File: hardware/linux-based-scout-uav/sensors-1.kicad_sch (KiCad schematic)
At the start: 1 part, among them U5 MPU-6050

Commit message: Schematic update
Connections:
- net I2C1_SCL: now reaches U5.23 (SCL)
- net I2C1_SDA: now reaches U5.24 (SDA)
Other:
- note added: "Sensors"
- moved on the sheet: U5
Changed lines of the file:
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@@
 	(wire
 		(pts
-			(xy 228.6 157.48) (xy 228.6 170.18)
+			(xy 92.71 148.59) (xy 92.71 161.29)
 		)
 		(stroke
@@
 		)
 	)
+	(wire
+		(pts
+			(xy 57.15 123.19) (xy 74.93 123.19)
+		)
+		(stroke
+			(width 0)
+			(type default)
+		)
+	)
+	(wire
+		(pts
+			(xy 57.15 125.73) (xy 74.93 125.73)
+		)
+		(stroke
+			(width 0)
+			(type default)
+		)
+	)
+	(text "Sensors"
+		(exclude_from_sim no)
+		(at 213.36 32.766 0)
+		(effects
+			(font
+				(face "KiCad Font")
+				(size 10.16 10.16)
+			)
+		)
+	)
+	(global_label "I2C1_SDA"
+		(shape bidirectional)
+		(at 57.15 123.19 180)
+		(fields_autoplaced yes)
+		(effects
+			(font
+				(size 1.27 1.27)
+			)
+			(justify right)
+		)
+		(property "Intersheetrefs" "${INTERSHEET_REFS}"
+			(at 44.224 123.19 0)
+			(effects
+				(font
+					(size 1.27 1.27)
+				)
+				(justify right)
+				(hide yes)
+			)
+		)
+	)
+	(global_label "I2C1_SCL"
+		(shape input)
+		(at 57.15 125.73 180)
+		(fields_autoplaced yes)
+		(effects
+			(font
+				(size 1.27 1.27)
+			)
+			(justify right)
+		)
+		(property "Intersheetrefs" "${INTERSHEET_REFS}"
+			(at 45.3958 125.73 0)
+			(effects
+				(font
+					(size 1.27 1.27)
+				)
+				(justify right)
+				(hide yes)
+			)
+		)
+	)
 	(symbol
 		(lib_id "Sensor_Motion:MPU-6050")
-		(at 228.6 139.7 0)
+		(at 92.71 130.81 0)
 		(unit 1)
 		(exclude_from_sim no)
@@
 		(fields_autoplaced yes)
 		(property "Reference" "U5"
-			(at 230.7941 156.21 0)
+			(at 94.9041 147.32 0)
 			(effects
 				(font
@@
 		)
 		(property "Value" "MPU-6050"
-			(at 230.7941 158.75 0)
+			(at 94.9041 149.86 0)
 			(effects
 				(font
@@
 		)
 		(property "Footprint" "Sensor_Motion:InvenSense_QFN-24_4x4mm_P0.5mm"
-			(at 228.6 160.02 0)
+			(at 92.71 151.13 0)
 			(effects
 				(font
@@
 		)
 		(property "Datasheet" "https://invensense.tdk.com/wp-content/uploads/2015/02/MPU-6000-Datasheet1.pdf"
-			(at 228.6 143.51 0)
+			(at 92.71 134.62 0)
 			(effects
 				(font
@@
 		)
 		(property "Description" "InvenSense 6-Axis Motion Sensor, Gyroscope, Accelerometer, I2C"
-			(at 228.6 139.7 0)
+			(at 92.71 130.81 0)
 			(effects
 				(font
@@
 	(symbol
 		(lib_id "power:GND")
-		(at 228.6 170.18 0)
+		(at 92.71 161.29 0)
 		(unit 1)
 		(exclude_from_sim no)
@@
 		(fields_autoplaced yes)
 		(property "Reference" "#PWR017"
-			(at 228.6 176.53 0)
+			(at 92.71 167.64 0)
 			(effects
 				(font
@@
 		)
 		(property "Value" "GND"
-			(at 228.6 175.26 0)
+			(at 92.71 166.37 0)
 			(effects
 				(font
@@
 		)
 		(property "Footprint" ""
-			(at 228.6 170.18 0)
+			(at 92.71 161.29 0)
 			(effects
 				(font
@@
 		)
 		(property "Datasheet" ""
-			(at 228.6 170.18 0)
+			(at 92.71 161.29 0)
 			(effects
 				(font
@@
 		)
 		(property "Description" "Power symbol creates a global label with name \"GND\" , ground"
-			(at 228.6 170.18 0)
-			(effects
-				(font
+			(at 92.71 161.29 0)
+			(effects
+				(font

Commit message: Schematic update
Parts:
- added R10: 10K, Resistor_SMD:R_0402_1005Metric, symbol Device:R
- added R11, R12: 10K DNP, Resistor_SMD:R_0402_1005Metric, symbol Device:R
- added U6: AMG8833, AMG8833:XDCR_AMG8833, symbol AMG8833:AMG8833
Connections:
- net GND: now also R11.2, U6.6 (GND)
- new net: R12.2, U6.4 (INT)
- new net: R10.2, R11.1, U6.5 (AD_SELECT)
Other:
- note added: "MPU-6050"
- moved on the sheet: U5

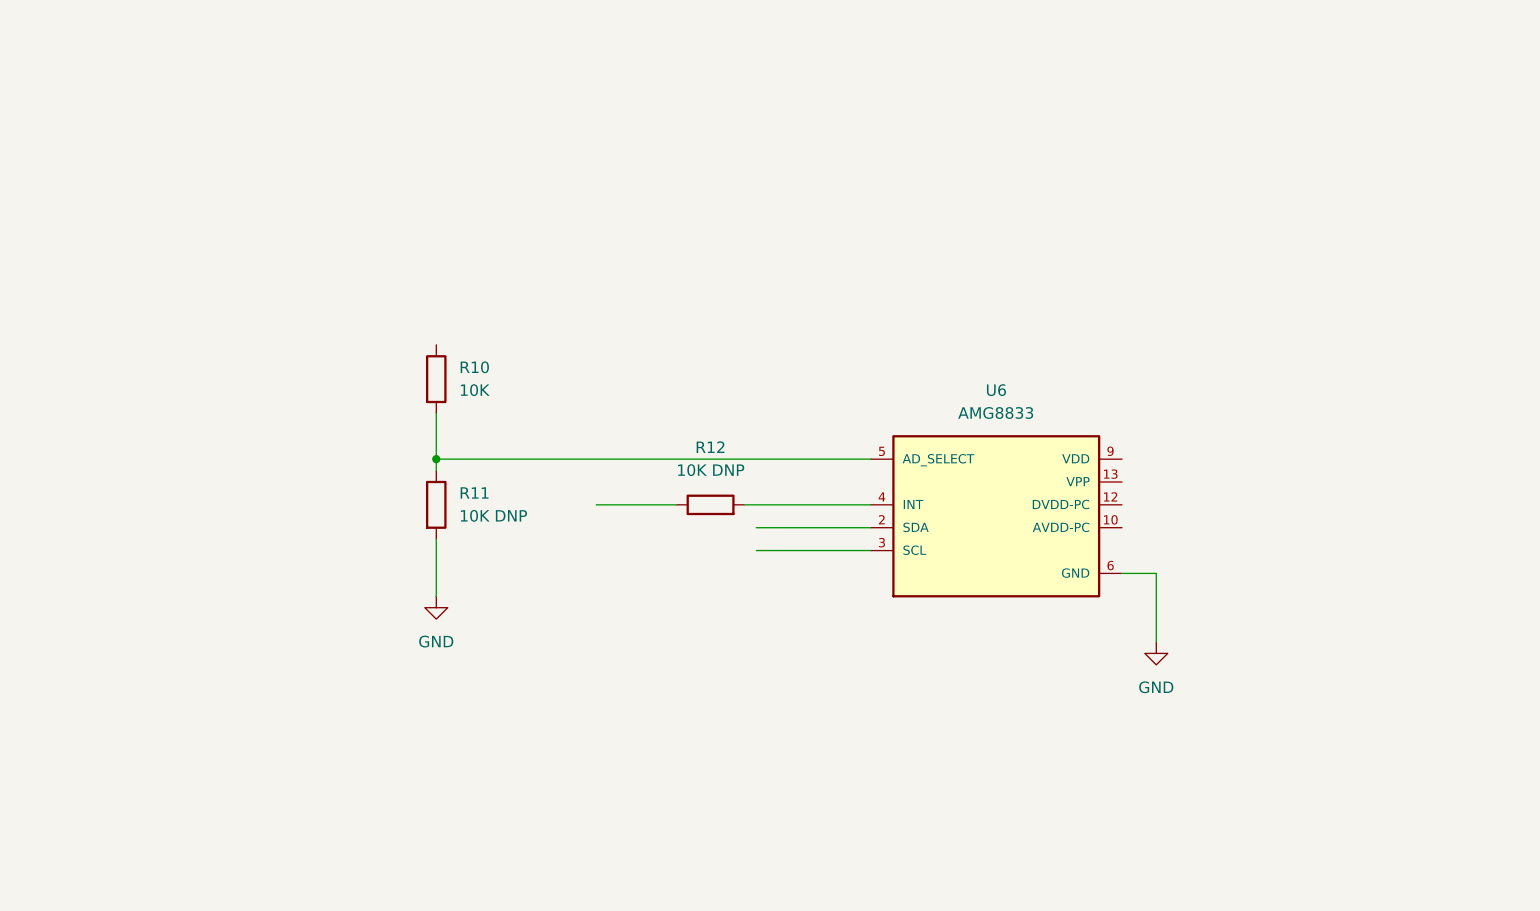
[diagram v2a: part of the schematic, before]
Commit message: Shcematic, board update.
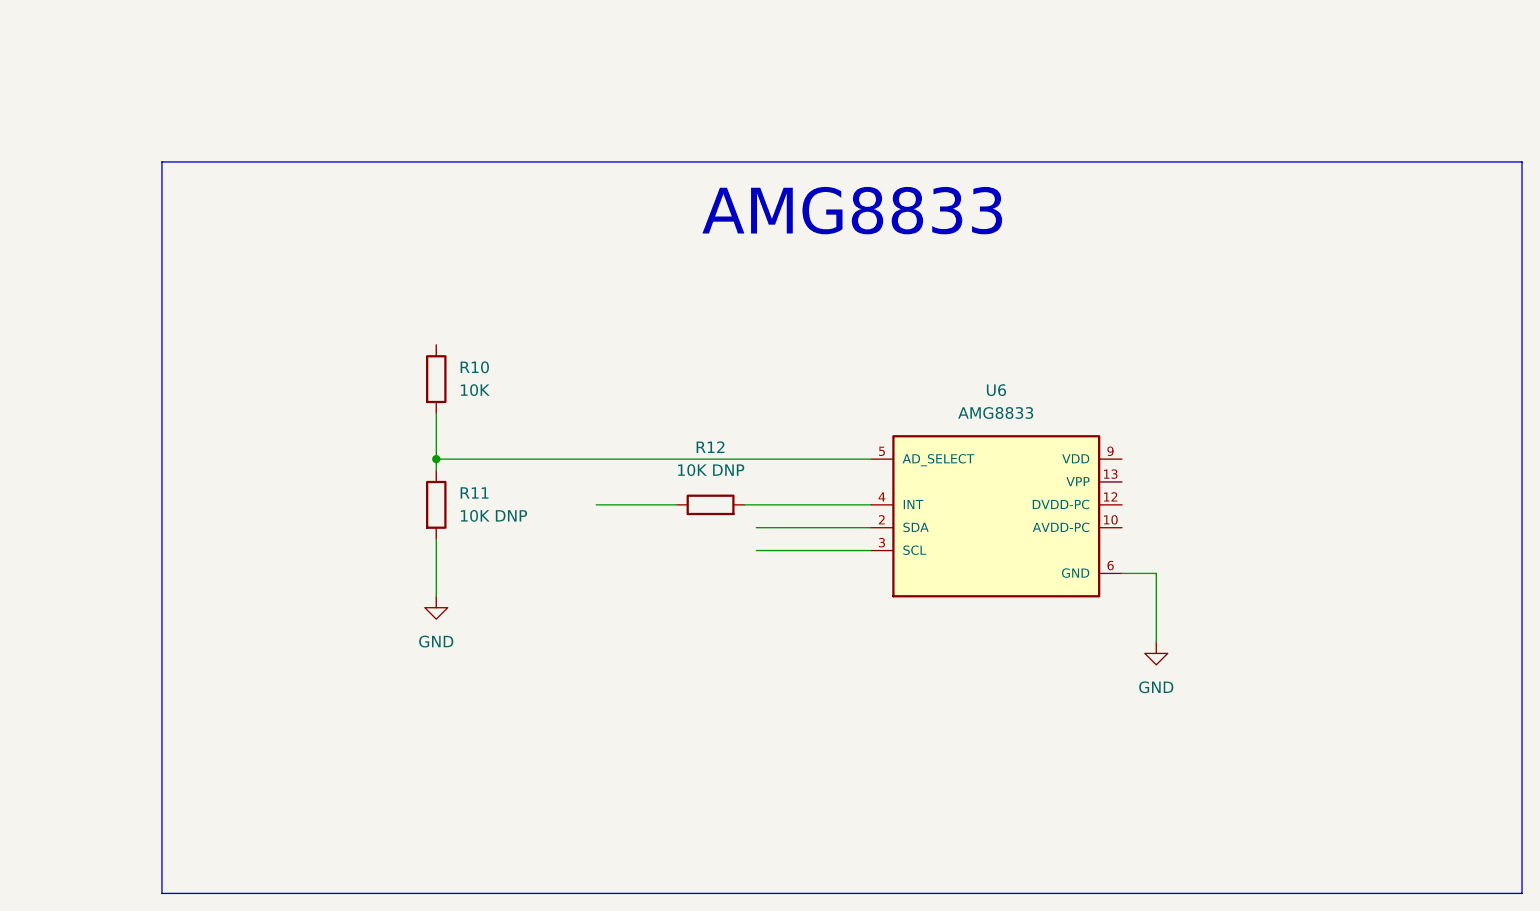
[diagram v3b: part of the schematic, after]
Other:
- note added: "AMG8833"
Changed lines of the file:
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@@
+		)
+	)
+	(rectangle
+		(start 195.58 92.71)
+		(end 346.71 173.99)
+		(stroke
+			(width 0)
+			(type default)
+		)
+		(fill
+			(type none)
+		)
+	)
+	(text "AMG8833"
+		(exclude_from_sim no)
+		(at 272.542 98.552 0)
+		(effects
+			(font
+				(size 5.08 5.08)
+			)
 		)
 	)

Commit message: Schematic update
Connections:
- net I2C1_SCL: now also U6.3 (SCL)
- net I2C1_SDA: now also U6.2 (SDA)
- net AMG833_INT: now reaches R12.1
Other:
- moved on the sheet: R10, R11, R12, U6

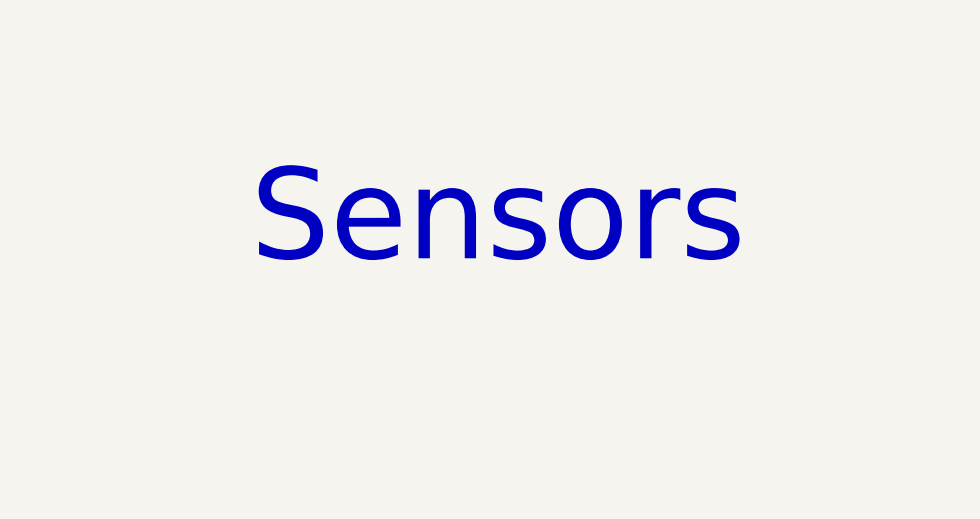
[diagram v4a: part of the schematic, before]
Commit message: Schematic update - eMMC added
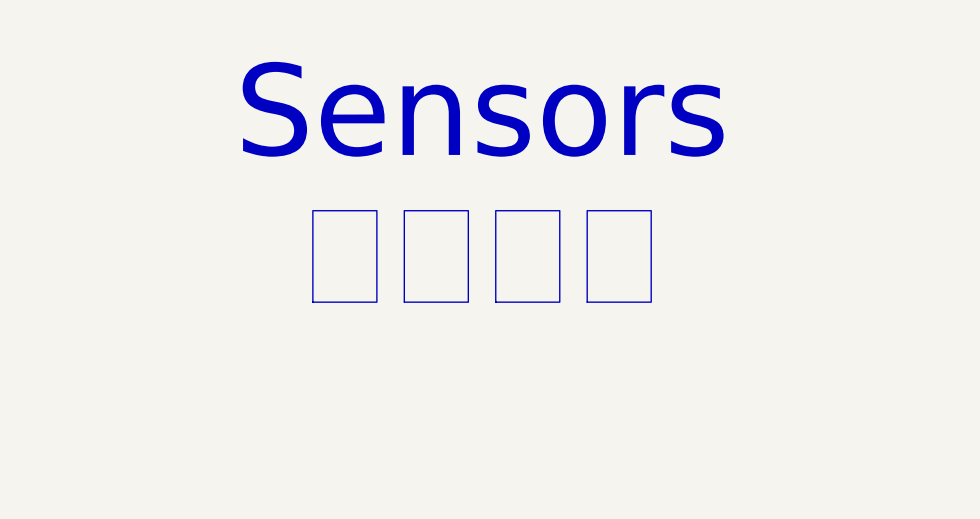
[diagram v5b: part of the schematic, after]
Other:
- note added: "Sensors センサー"
- note removed: "Sensors"
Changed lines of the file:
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@@
 		)
 	)
-	(text "Sensors"
+	(text "Sensors\nセンサー"
 		(exclude_from_sim no)
-		(at 213.36 32.766 0)
+		(at 211.582 29.464 0)
 		(effects
 			(font

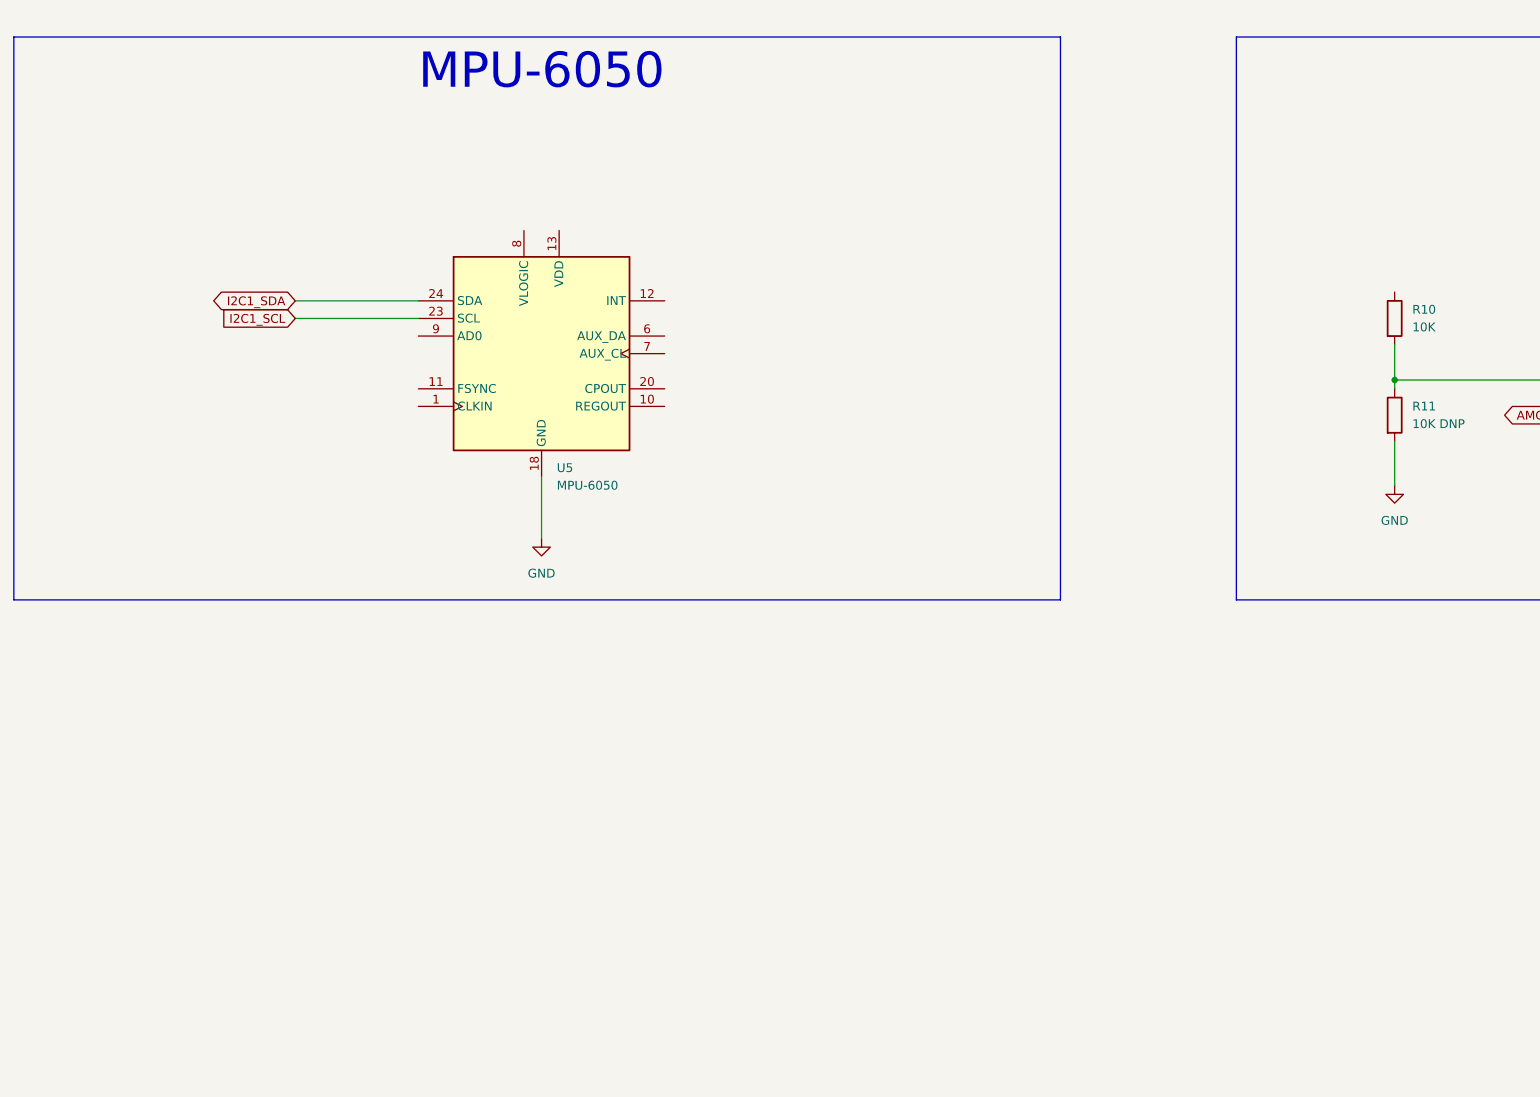
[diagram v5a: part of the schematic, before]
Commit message: Schematic update
Work around I2C sensors
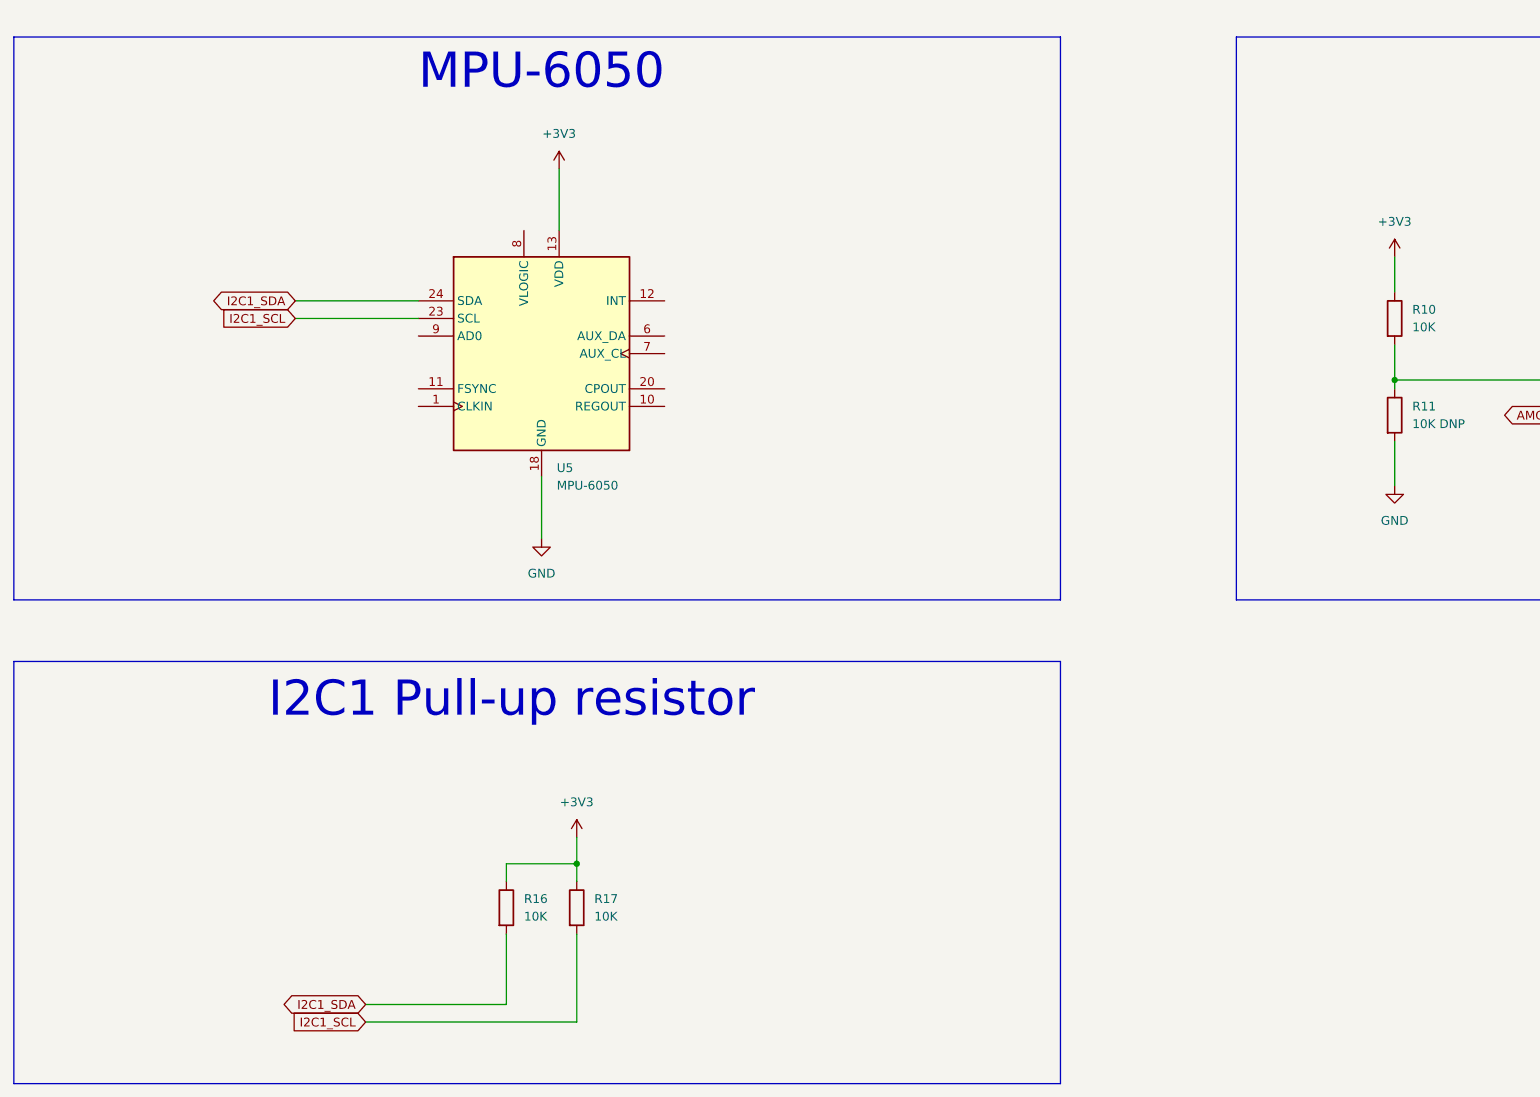
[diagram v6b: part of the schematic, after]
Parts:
- added R16, R17: 10K, Resistor_SMD:R_0402_1005Metric, symbol Device:R
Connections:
- net I2C1_SCL: now also R17.2
- net I2C1_SDA: now also R16.2
- net +3V3: now reaches R10.1
- net +3V3: now also U5.13 (VDD), R16.1, R17.1
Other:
- note added: "I2C1 Pull-up resistor"
